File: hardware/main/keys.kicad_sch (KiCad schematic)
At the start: 134 parts, among them SW1 Esc, SW10 a, SW12 Fn, SW13 F2, SW14 2, SW15 w, SW16 s, SW17 z, SW18 Tux, SW19 F3, SW2 F1, SW20 3, SW21 e, SW22 d, SW23 c, SW24 Alt, SW25 F4, SW26 4, SW27 r, SW28 f, SW29 v, SW3 tilde, SW31 F5, SW32 5, SW33 t, SW34 g, SW35 b, SW36 F6, SW37 6, SW38 y, SW39 h, SW4 Tab, SW40 n, SW41 F7, SW42 7, SW43 u, SW44 j, SW45 m, SW46 Space, SW47 F8, SW48 8, SW49 i, SW5 Caps Lock, SW50 k, SW51 comma, SW52 F9, SW53 9, SW54 o, SW55 l, SW56 dot, SW57 F10, SW58 0, SW59 p, SW6 Shift, SW60 semicolon, SW61 slash, SW62 Alt Gr, SW63 F11, SW64 minus, SW65 sq br open, SW66 apostrophe, SW68 F12, SW69 equal, SW7 Ctrl, SW70 sq br close, SW71 backslash, SW72 Shift, SW73 Ctrl, SW74 Print, SW75 Backspace, SW76 Enter, SW77 Left, SW78 Scroll Lock, SW79 Up, SW8 1, SW80 Down, SW81 Pause, SW82 INS, SW83 DEL, SW84 Page Up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

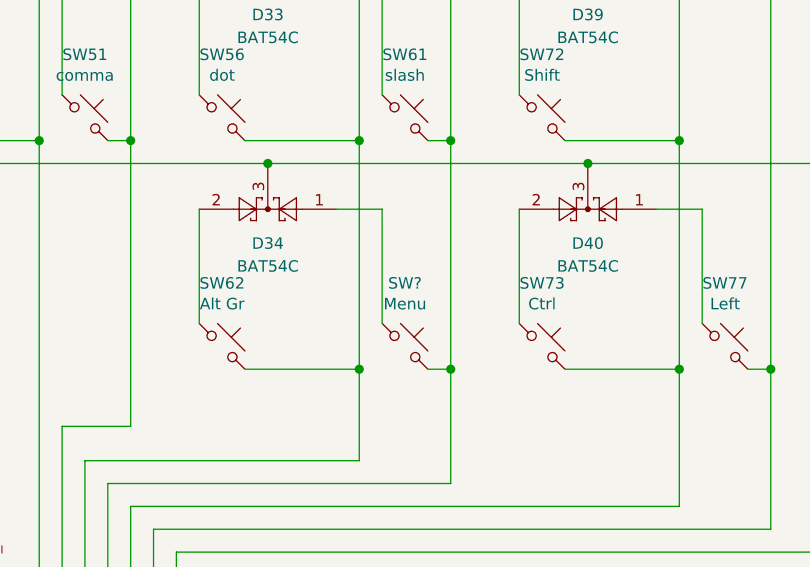
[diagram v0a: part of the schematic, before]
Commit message: Add switch to choose the connection type
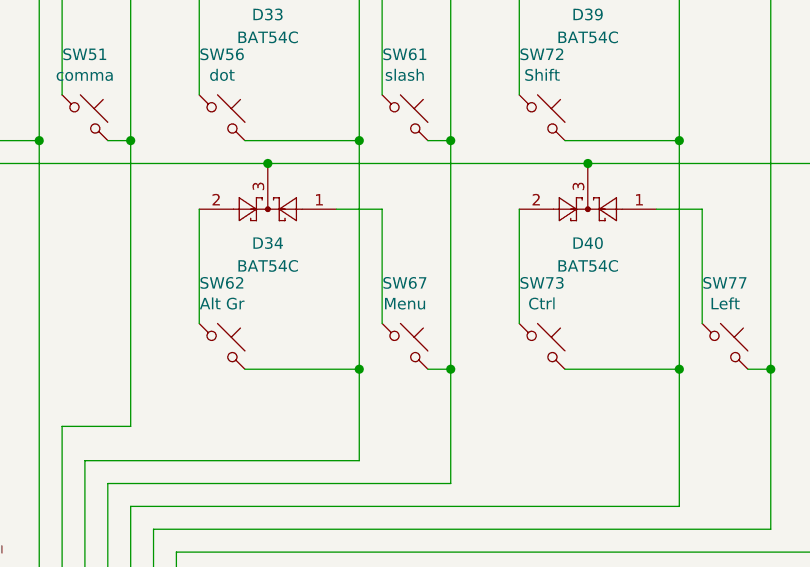
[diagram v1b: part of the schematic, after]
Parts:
- gave numbers to parts that had none: 1
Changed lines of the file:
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@@
-(kicad_sch (version 20201015) (generator eeschema)
+(kicad_sch (version 20210123) (generator eeschema)
   (paper "A3")
   (junction (at 27.94 58.42) (diameter 1.016) (color 0 0 0 0))
@@
   (symbol (lib_id "Switch:SW_Push_45deg") (at 289.56 177.8 0) (unit 1)
     (in_bom yes) (on_board yes)
-    (property "Reference" "SW?" (id 0) (at 289.56 170.7958 0))
+    (property "Reference" "SW67" (id 0) (at 289.56 170.7958 0))
     (property "Value" "Menu" (id 1) (at 289.56 173.095 0))
     (property "Footprint" "footprints:SW_Cherry_MX_1.00u_PCB" (id 2) (at 289.56 177.8 0)

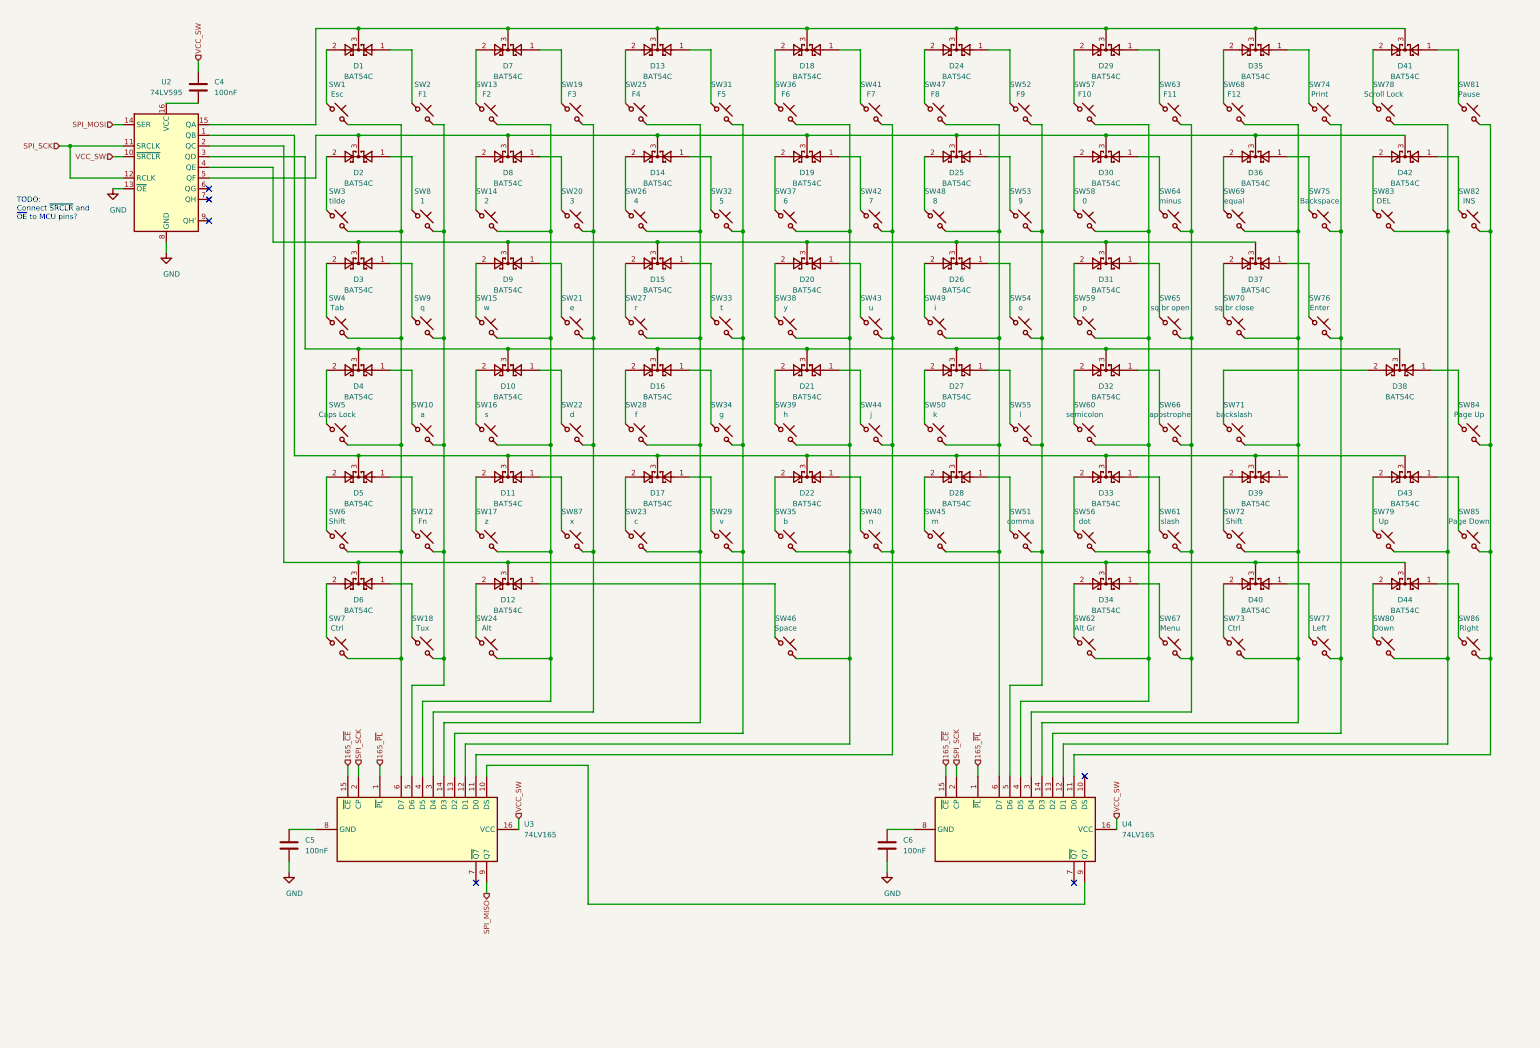
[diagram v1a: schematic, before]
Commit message: Fix errors found by ERC
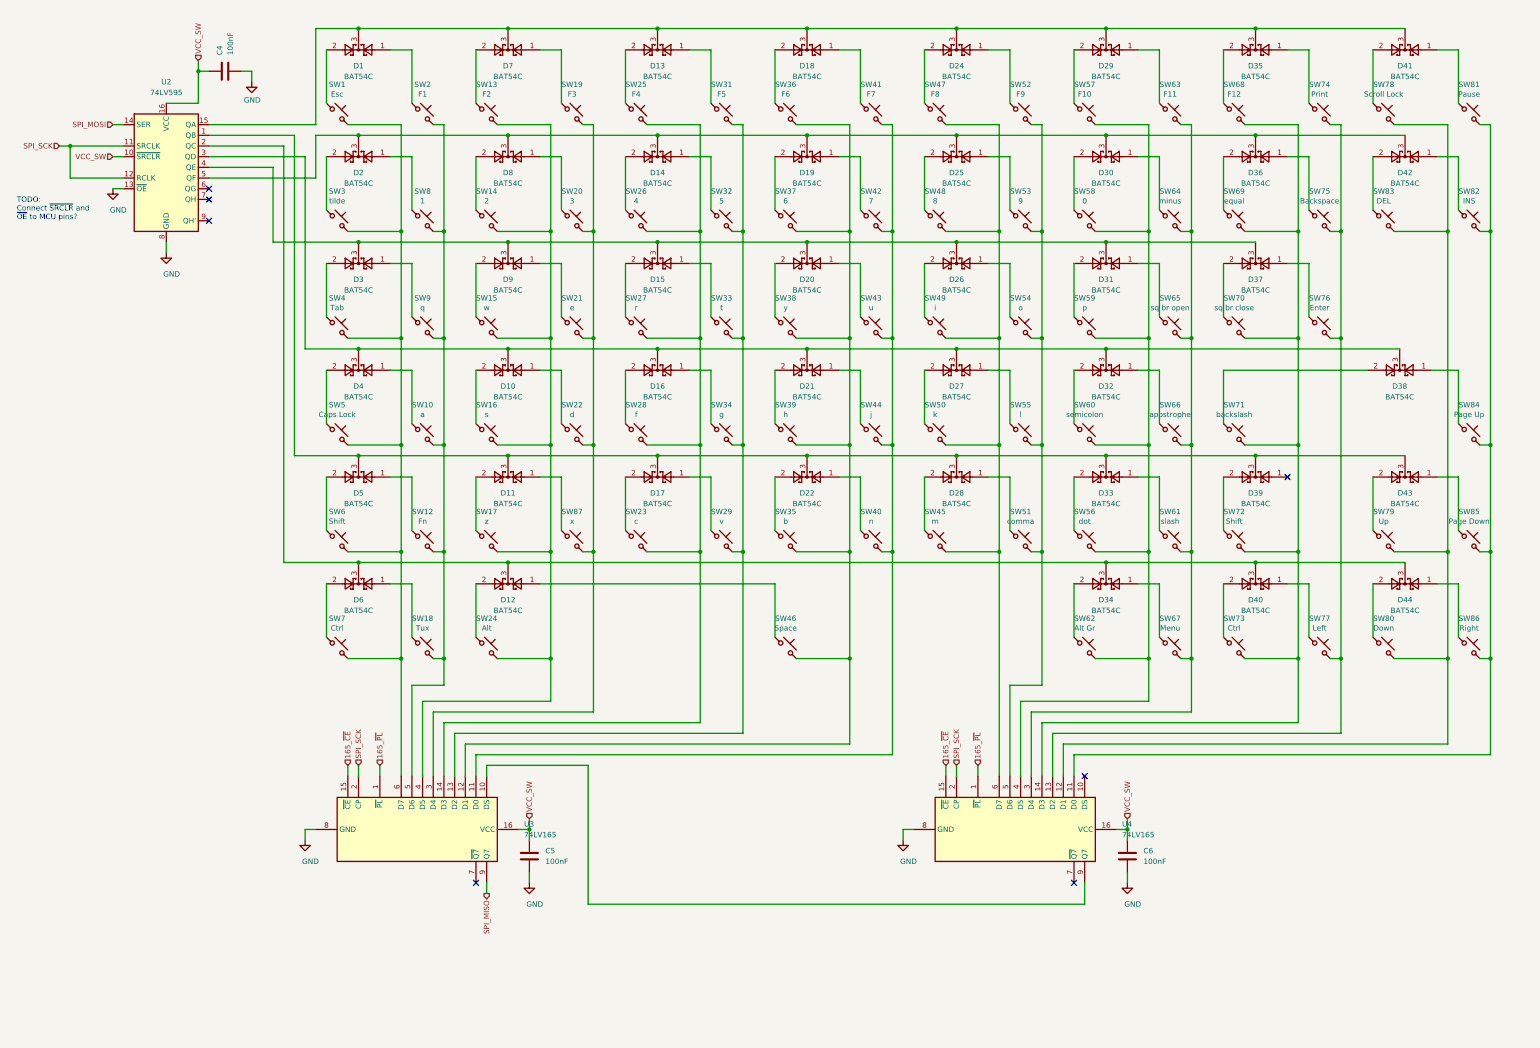
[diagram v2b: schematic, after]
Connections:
- net GND: now also C4.2, U3.8 (GND), U4.8 (GND)
- net VCC_SW: now also C5.1, C6.1, U2.16 (VCC)
- no-connect marks 6 -> 7
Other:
- moved on the sheet: C4, C5

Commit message: WIP: Design of PCB
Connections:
- net at SW1.2, SW3.2, SW4.2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: now also U3.5 (D6); no longer U3.6 (D7)
- net at SW10.2, SW12.2, SW18.2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: now also U3.6 (D7); no longer U3.5 (D6)
- net at D11.3, D17.3, D22.3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: now also U2.7 (QH); no longer U2.1 (QB)
- net at D1.3, D13.3, D18.3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: now also U2.2 (QC); no longer U2.15 (QA)
- net at D12.3, D34.3, D40.3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: now also U2.6 (QG); no longer U2.2 (QC)
- net at D14.3, D19.3, D2.3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: now also U2.1 (QB); no longer U2.5 (QF)
- net at SW45.2, SW47.2, SW48.2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: now also U4.5 (D6); no longer U4.6 (D7)
- net at SW51.2, SW52.2, SW53.2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: now also U4.6 (D7); no longer U4.5 (D6)
- net at D10.3, D16.3, D21.3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: now also U2.4 (QE); no longer U2.3 (QD)
- net at D15.3, D20.3, D26.3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: now also U2.3 (QD); no longer U2.4 (QE)
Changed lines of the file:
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@@
   (junction (at 365.76 154.94) (diameter 1.016) (color 0 0 0 0))
   (junction (at 365.76 180.34) (diameter 1.016) (color 0 0 0 0))
-  (no_connect (at 60.96 68.58))
-  (no_connect (at 60.96 71.12))
+  (no_connect (at 60.96 53.34))
+  (no_connect (at 60.96 66.04))
   (no_connect (at 60.96 76.2))
   (no_connect (at 124.46 233.68))
@@
     (stroke (width 0) (type solid) (color 0 0 0 0))
   )
-  (wire (pts (xy 60.96 55.88) (xy 81.28 55.88))
-    (stroke (width 0) (type solid) (color 0 0 0 0))
-  )
-  (wire (pts (xy 60.96 58.42) (xy 78.74 58.42))
-    (stroke (width 0) (type solid) (color 0 0 0 0))
-  )
-  (wire (pts (xy 60.96 60.96) (xy 83.82 60.96))
-    (stroke (width 0) (type solid) (color 0 0 0 0))
-  )
-  (wire (pts (xy 60.96 63.5) (xy 76.2 63.5))
-    (stroke (width 0) (type solid) (color 0 0 0 0))
-  )
-  (wire (pts (xy 60.96 66.04) (xy 86.36 66.04))
+  (wire (pts (xy 60.96 55.88) (xy 96.52 55.88))
+    (stroke (width 0) (type solid) (color 0 0 0 0))
+  )
+  (wire (pts (xy 60.96 58.42) (xy 81.28 58.42))
+    (stroke (width 0) (type solid) (color 0 0 0 0))
+  )
+  (wire (pts (xy 60.96 60.96) (xy 81.28 60.96))
+    (stroke (width 0) (type solid) (color 0 0 0 0))
+  )
+  (wire (pts (xy 60.96 63.5) (xy 78.74 63.5))
+    (stroke (width 0) (type solid) (color 0 0 0 0))
+  )
+  (wire (pts (xy 60.96 68.58) (xy 73.66 68.58))
     (stroke (width 0) (type solid) (color 0 0 0 0))
   )
@@
     (stroke (width 0) (type solid) (color 0 0 0 0))
   )
-  (wire (pts (xy 76.2 81.28) (xy 76.2 63.5))
-    (stroke (width 0) (type solid) (color 0 0 0 0))
-  )
-  (wire (pts (xy 76.2 81.28) (xy 96.52 81.28))
-    (stroke (width 0) (type solid) (color 0 0 0 0))
-  )
-  (wire (pts (xy 78.74 58.42) (xy 78.74 157.48))
-    (stroke (width 0) (type solid) (color 0 0 0 0))
-  )
-  (wire (pts (xy 78.74 157.48) (xy 96.52 157.48))
-    (stroke (width 0) (type solid) (color 0 0 0 0))
-  )
-  (wire (pts (xy 81.28 55.88) (xy 81.28 132.08))
-    (stroke (width 0) (type solid) (color 0 0 0 0))
-  )
-  (wire (pts (xy 81.28 132.08) (xy 96.52 132.08))
-    (stroke (width 0) (type solid) (color 0 0 0 0))
-  )
-  (wire (pts (xy 83.82 60.96) (xy 83.82 106.68))
-    (stroke (width 0) (type solid) (color 0 0 0 0))
-  )
-  (wire (pts (xy 83.82 106.68) (xy 96.52 106.68))
+  (wire (pts (xy 73.66 68.58) (xy 73.66 157.48))
+    (stroke (width 0) (type solid) (color 0 0 0 0))
+  )
+  (wire (pts (xy 73.66 157.48) (xy 96.52 157.48))
+    (stroke (width 0) (type solid) (color 0 0 0 0))
+  )
+  (wire (pts (xy 76.2 71.12) (xy 60.96 71.12))
+    (stroke (width 0) (type solid) (color 0 0 0 0))
+  )
+  (wire (pts (xy 76.2 132.08) (xy 76.2 71.12))
+    (stroke (width 0) (type solid) (color 0 0 0 0))
+  )
+  (wire (pts (xy 76.2 132.08) (xy 96.52 132.08))
+    (stroke (width 0) (type solid) (color 0 0 0 0))
+  )
+  (wire (pts (xy 78.74 63.5) (xy 78.74 106.68))
+    (stroke (width 0) (type solid) (color 0 0 0 0))
+  )
+  (wire (pts (xy 78.74 106.68) (xy 96.52 106.68))
+    (stroke (width 0) (type solid) (color 0 0 0 0))
+  )
+  (wire (pts (xy 81.28 30.48) (xy 81.28 58.42))
+    (stroke (width 0) (type solid) (color 0 0 0 0))
+  )
+  (wire (pts (xy 81.28 30.48) (xy 96.52 30.48))
+    (stroke (width 0) (type solid) (color 0 0 0 0))
+  )
+  (wire (pts (xy 81.28 60.96) (xy 81.28 81.28))
+    (stroke (width 0) (type solid) (color 0 0 0 0))
+  )
+  (wire (pts (xy 81.28 81.28) (xy 96.52 81.28))
     (stroke (width 0) (type solid) (color 0 0 0 0))
   )
@@
     (stroke (width 0) (type solid) (color 0 0 0 0))
   )
-  (wire (pts (xy 86.36 30.48) (xy 86.36 53.34))
-    (stroke (width 0) (type solid) (color 0 0 0 0))
-  )
-  (wire (pts (xy 86.36 53.34) (xy 60.96 53.34))
-    (stroke (width 0) (type solid) (color 0 0 0 0))
-  )
-  (wire (pts (xy 86.36 55.88) (xy 96.52 55.88))
-    (stroke (width 0) (type solid) (color 0 0 0 0))
-  )
-  (wire (pts (xy 86.36 66.04) (xy 86.36 55.88))
-    (stroke (width 0) (type solid) (color 0 0 0 0))
-  )
   (wire (pts (xy 88.9 35.56) (xy 88.9 48.26))
     (stroke (width 0) (type solid) (color 0 0 0 0))
@@
     (stroke (width 0) (type solid) (color 0 0 0 0))
   )
-  (wire (pts (xy 96.52 30.48) (xy 86.36 30.48))
-    (stroke (width 0) (type solid) (color 0 0 0 0))
-  )
   (wire (pts (xy 96.52 30.48) (xy 132.08 30.48))
     (stroke (width 0) (type solid) (color 0 0 0 0))
@@
     (stroke (width 0) (type solid) (color 0 0 0 0))
   )
-  (wire (pts (xy 106.68 180.34) (xy 106.68 208.28))
+  (wire (pts (xy 106.68 180.34) (xy 106.68 184.15))
+    (stroke (width 0) (type solid) (color 0 0 0 0))
+  )
+  (wire (pts (xy 106.68 186.69) (xy 116.84 186.69))
+    (stroke (width 0) (type solid) (color 0 0 0 0))
+  )
+  (wire (pts (xy 106.68 208.28) (xy 106.68 186.69))
     (stroke (width 0) (type solid) (color 0 0 0 0))
   )
@@
     (stroke (width 0) (type solid) (color 0 0 0 0))
   )
-  (wire (pts (xy 109.22 186.69) (xy 109.22 208.28))
+  (wire (pts (xy 109.22 184.15) (xy 106.68 184.15))
+    (stroke (width 0) (type solid) (color 0 0 0 0))
+  )
+  (wire (pts (xy 109.22 208.28) (xy 109.22 184.15))
     (stroke (width 0) (type solid) (color 0 0 0 0))
   )
@@
     (stroke (width 0) (type solid) (color 0 0 0 0))
   )
-  (wire (pts (xy 114.3 193.04) (xy 114.3 208.28))
+  (wire (pts (xy 114.3 193.04) (xy 152.4 193.04))
+    (stroke (width 0) (type solid) (color 0 0 0 0))
+  )
+  (wire (pts (xy 114.3 208.28) (xy 114.3 193.04))
     (stroke (width 0) (type solid) (color 0 0 0 0))
   )
@@
     (stroke (width 0) (type solid) (color 0 0 0 0))
   )
-  (wire (pts (xy 116.84 186.69) (xy 109.22 186.69))
-    (stroke (width 0) (type solid) (color 0 0 0 0))
-  )
   (wire (pts (xy 116.84 195.58) (xy 116.84 208.28))
     (stroke (width 0) (type solid) (color 0 0 0 0))
@@
     (stroke (width 0) (type solid) (color 0 0 0 0))
   )
-  (wire (pts (xy 152.4 193.04) (xy 114.3 193.04))
-    (stroke (width 0) (type solid) (color 0 0 0 0))
-  )
   (wire (pts (xy 160.02 35.56) (xy 160.02 48.26))
     (stroke (width 0) (type solid) (color 0 0 0 0))
@@
     (stroke (width 0) (type solid) (color 0 0 0 0))
   )
-  (wire (pts (xy 248.92 154.94) (xy 248.92 208.28))
+  (wire (pts (xy 248.92 186.69) (xy 248.92 208.28))
+    (stroke (width 0) (type solid) (color 0 0 0 0))
+  )
+  (wire (pts (xy 248.92 186.69) (xy 259.08 186.69))
     (stroke (width 0) (type solid) (color 0 0 0 0))
   )
@@
     (stroke (width 0) (type solid) (color 0 0 0 0))
   )
-  (wire (pts (xy 251.46 186.69) (xy 251.46 208.28))
+  (wire (pts (xy 251.46 154.94) (xy 248.92 154.94))
+    (stroke (width 0) (type solid) (color 0 0 0 0))
+  )
+  (wire (pts (xy 251.46 208.28) (xy 251.46 154.94))
     (stroke (width 0) (type solid) (color 0 0 0 0))
   )
@@
     (stroke (width 0) (type solid) (color 0 0 0 0))
   )
-  (wire (pts (xy 259.08 186.69) (xy 251.46 186.69))
-    (stroke (width 0) (type solid) (color 0 0 0 0))
-  )

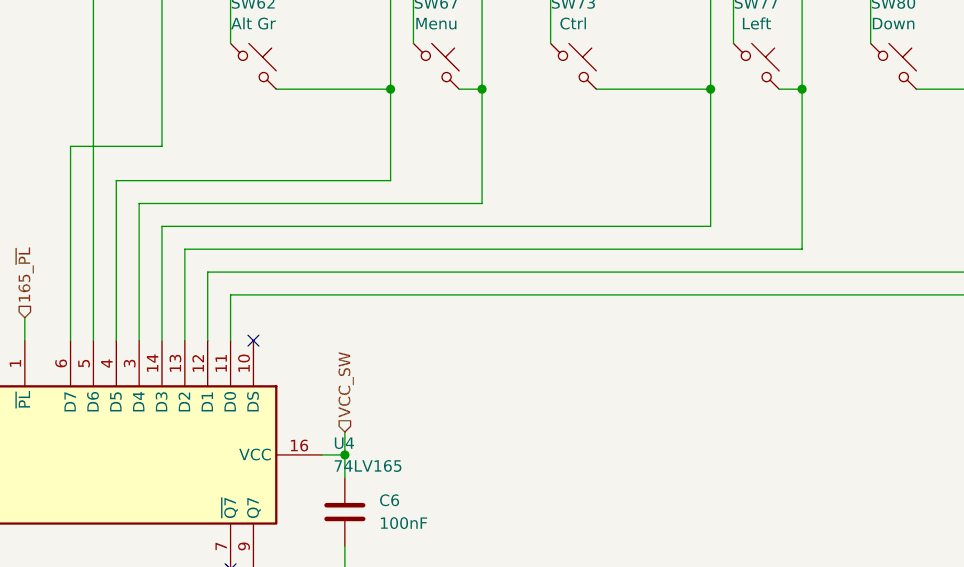
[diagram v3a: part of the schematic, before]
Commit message: Route traces for the shift registers
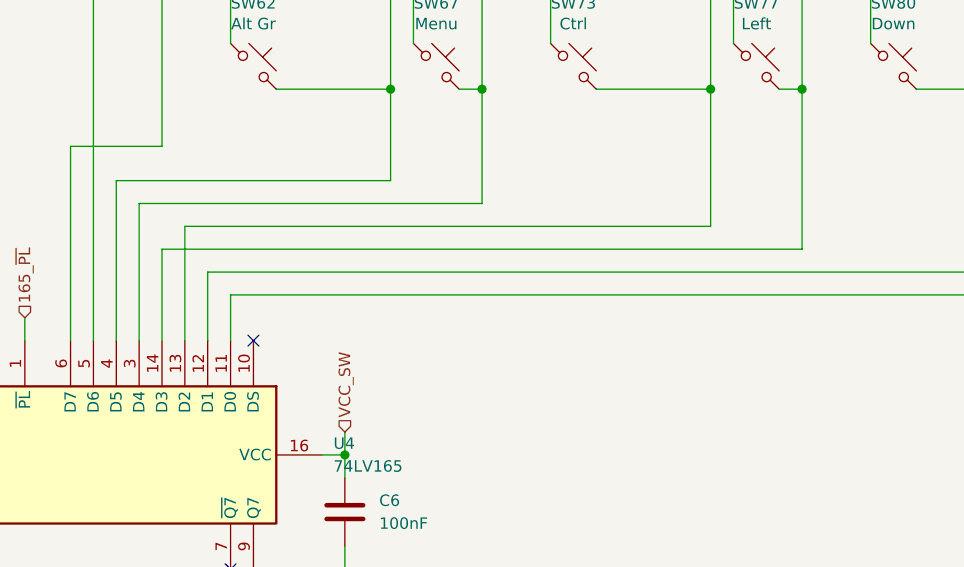
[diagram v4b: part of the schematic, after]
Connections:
- net at SW68.2, SW69.2, SW70.2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: now also U4.13 (D2); no longer U4.14 (D3)
- net at SW74.2, SW75.2, SW76.2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: now also U4.14 (D3); no longer U4.13 (D2)
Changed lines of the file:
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@@
     (stroke (width 0) (type solid) (color 0 0 0 0))
   )
-  (wire (pts (xy 259.08 195.58) (xy 259.08 208.28))
-    (stroke (width 0) (type solid) (color 0 0 0 0))
-  )
-  (wire (pts (xy 261.62 198.12) (xy 330.2 198.12))
-    (stroke (width 0) (type solid) (color 0 0 0 0))
-  )
-  (wire (pts (xy 261.62 208.28) (xy 261.62 198.12))
+  (wire (pts (xy 259.08 198.12) (xy 330.2 198.12))
+    (stroke (width 0) (type solid) (color 0 0 0 0))
+  )
+  (wire (pts (xy 259.08 208.28) (xy 259.08 198.12))
+    (stroke (width 0) (type solid) (color 0 0 0 0))
+  )
+  (wire (pts (xy 261.62 195.58) (xy 261.62 208.28))
     (stroke (width 0) (type solid) (color 0 0 0 0))
   )
@@
     (stroke (width 0) (type solid) (color 0 0 0 0))
   )
-  (wire (pts (xy 320.04 195.58) (xy 259.08 195.58))
-    (stroke (width 0) (type solid) (color 0 0 0 0))
-  )
+  (wire (pts (xy 320.04 195.58) (xy 261.62 195.58))
+    (stroke (width 0) (type solid) (color 0 0 0 0))
+  )
